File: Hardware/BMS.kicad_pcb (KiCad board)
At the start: 4 copper layers, 109 x 148 mm, 369 parts, among them IC1 STM32H742VIT6, IC2 TPS563200DDCR, J1 Conn_01x28, J10 Conn_01x10, J11 USB4235-03-C_REVA, J13 USB_A, J16 Conn_01x10, J19 Conn_02x13_Counter_Clockwise, J7 FTSH-107-01-L-D-K, Q2 100V/2W, Q5 DMT6018LDR-7, Q7 DMT6018LDR-7, Q8 100V/2W, SW1 SW_Push, U1 BQ79614PAPRQ1, U2 BQ79614PAPRQ1, U3 PBQ79600PWQ1, U4 MCP2542FD-E/MF, U5 PTPSM863253RDXR

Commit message: Male zmiany
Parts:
- moved G*** 1.30 mm to (142.1, 45.8)
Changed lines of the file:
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@@
 		(tags "capacitor handsolder")
 		(property "Reference" "C48"
-			(at -2.375 -0.1 270)
+			(at -2.05 -0.075 270)
 			(layer "F.SilkS")
 			(effects
 				(font
-					(size 0.5 0.5)
-					(thickness 0.125)
+					(size 0.3 0.3)
+					(thickness 0.06)
 					(bold yes)
 				)
@@
 		(tags "resistor handsolder")
 		(property "Reference" "R51"
-			(at -2.375 0 270)
+			(at -2.05 0 270)
 			(layer "F.SilkS")
 			(effects
 				(font
-					(size 0.5 0.5)
-					(thickness 0.125)
+					(size 0.3 0.3)
+					(thickness 0.06)
 					(bold yes)
 				)
@@
 	(footprint "footrpint:cat2_15x15"
 		(layer "F.Cu")
-		(at 143.40177 45.854048)
+		(at 142.10177 45.826153)
 		(property "Reference" "G***"
 			(at 0 0 0)
@@
 		(tags "capacitor handsolder")
 		(property "Reference" "C49"
-			(at -2.375 0.1 270)
+			(at -2.05 0.05 270)
 			(layer "F.SilkS")
 			(effects
 				(font
-					(size 0.5 0.5)
-					(thickness 0.125)
-					(bold yes)
+					(size 0.3 0.3)
+					(thickness 0.0375)
 				)
 			)
@@
 		(tags "MOSFET (N-Channel)")
 		(property "Reference" "Q5"
-			(at 0 0 0)
+			(at -2.275 -2.79375 0)
 			(layer "F.SilkS")
 			(effects
 				(font
-					(size 1.27 1.27)
-					(thickness 0.254)
+					(size 0.5 0.5)
+					(thickness 0.125)
+					(bold yes)
 				)
 			)

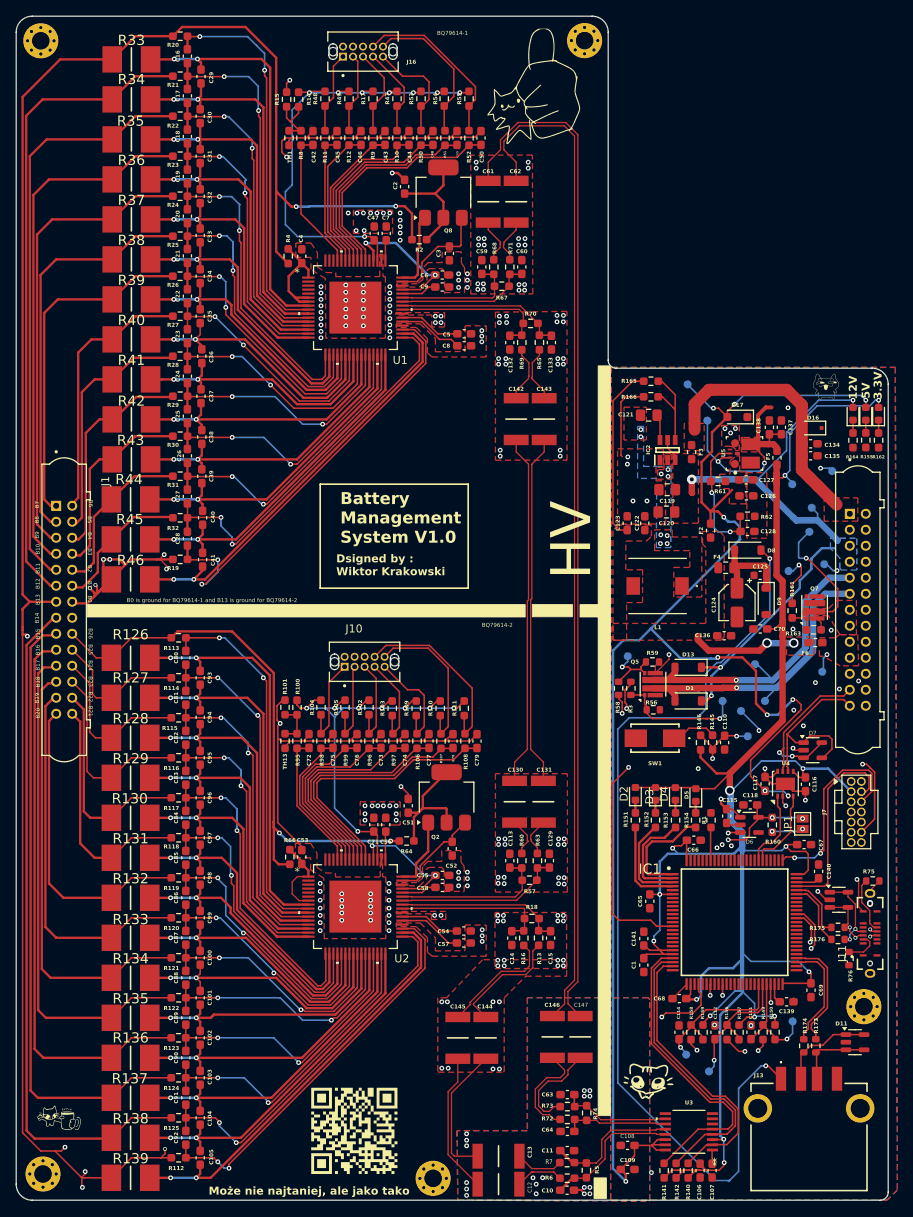
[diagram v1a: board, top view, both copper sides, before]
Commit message: Fixed boot resistor ground
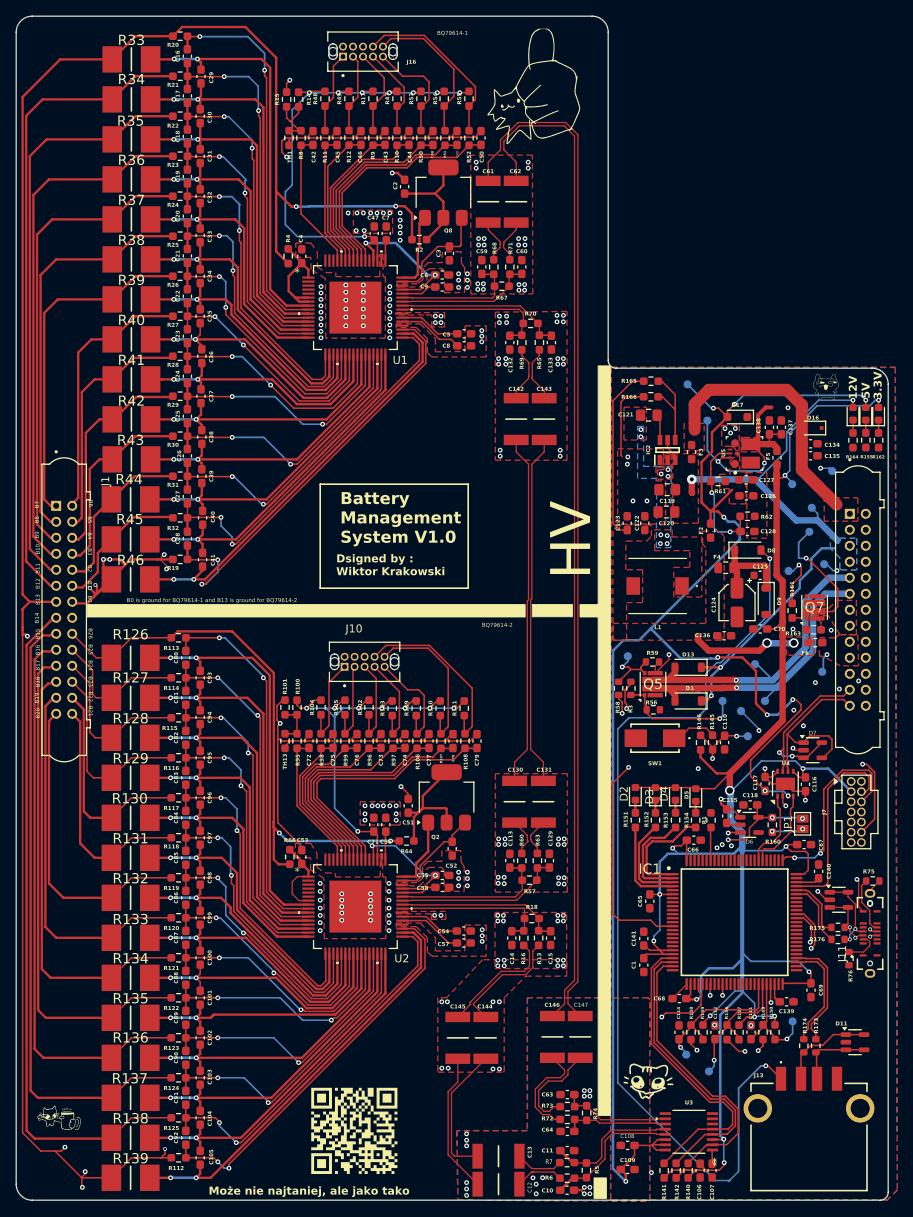
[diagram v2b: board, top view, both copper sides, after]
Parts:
- removed REF** (x5): MountingHole_2.2mm_M2_Pad_Via, MountingHole:MountingHole_2.2mm_M2_Pad_Via
- R164: value 300 -> 1k
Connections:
- R1 pad 1: Net-(R1-Pad1) -> GND

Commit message: zmiany w kodzier bq
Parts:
- added H1: MountingHole, MountingHole:MountingHole_2.2mm_M2_Pad_Via, F.Cu at (80.9, 39.9)
- added H2: MountingHole, MountingHole:MountingHole_2.2mm_M2_Pad_Via, F.Cu at (148.9, 39.9)
- added H3: MountingHole, MountingHole:MountingHole_2.2mm_M2_Pad_Via, F.Cu at (80.9, 181.9)
- added H4: MountingHole, MountingHole:MountingHole_2.2mm_M2_Pad_Via, F.Cu at (130.4, 181.9)
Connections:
- R1 pad 1: GND -> Net-(R1-Pad1)
